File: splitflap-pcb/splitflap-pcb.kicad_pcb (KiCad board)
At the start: 2 copper layers, 50 x 32 mm, 16 parts, among them J1 INPUT CONN, J2 HALL 1, J3 HALL 2, J4 STEPPER 1, J5 STEPPER 2, J6 OUTPUT CONN, J7 AVR-ISP-6, U1 REGULATOR, U2 ATtiny88-AU, U3 TPIC6595

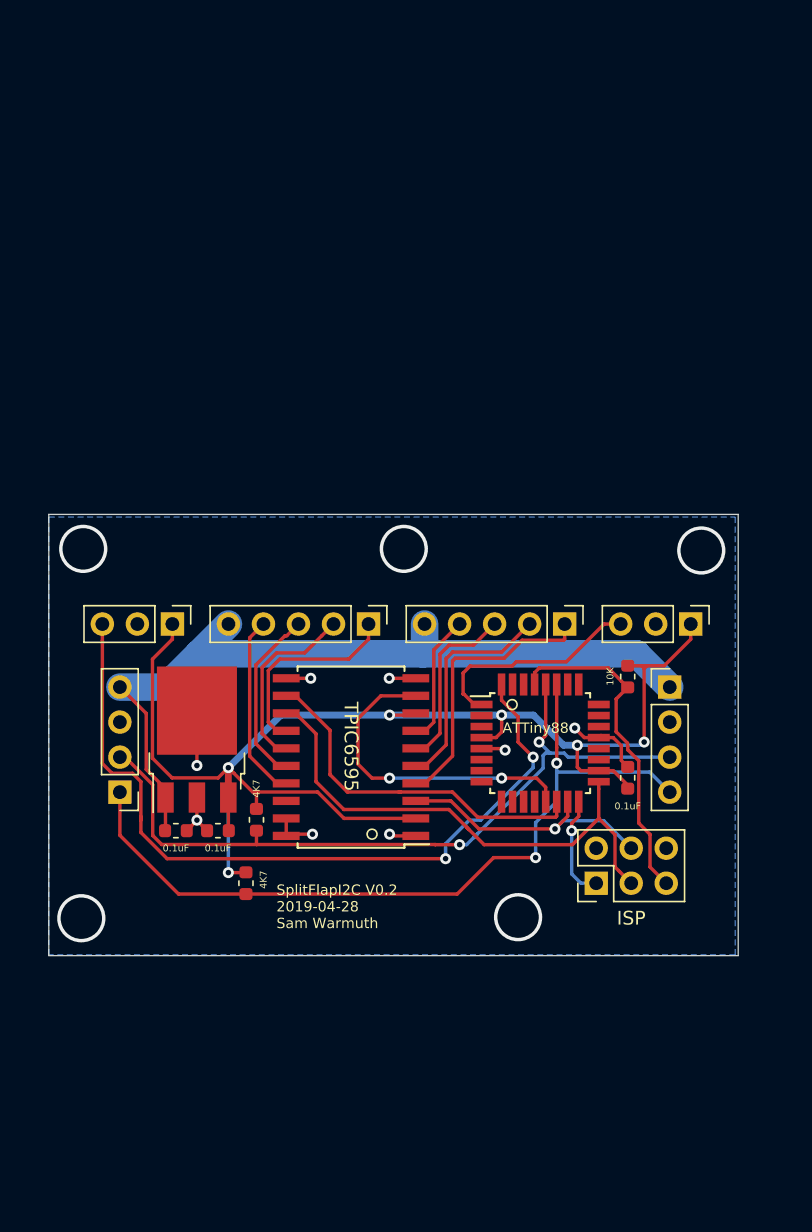
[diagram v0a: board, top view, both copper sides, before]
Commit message: Redesign PCB, connectors are too big
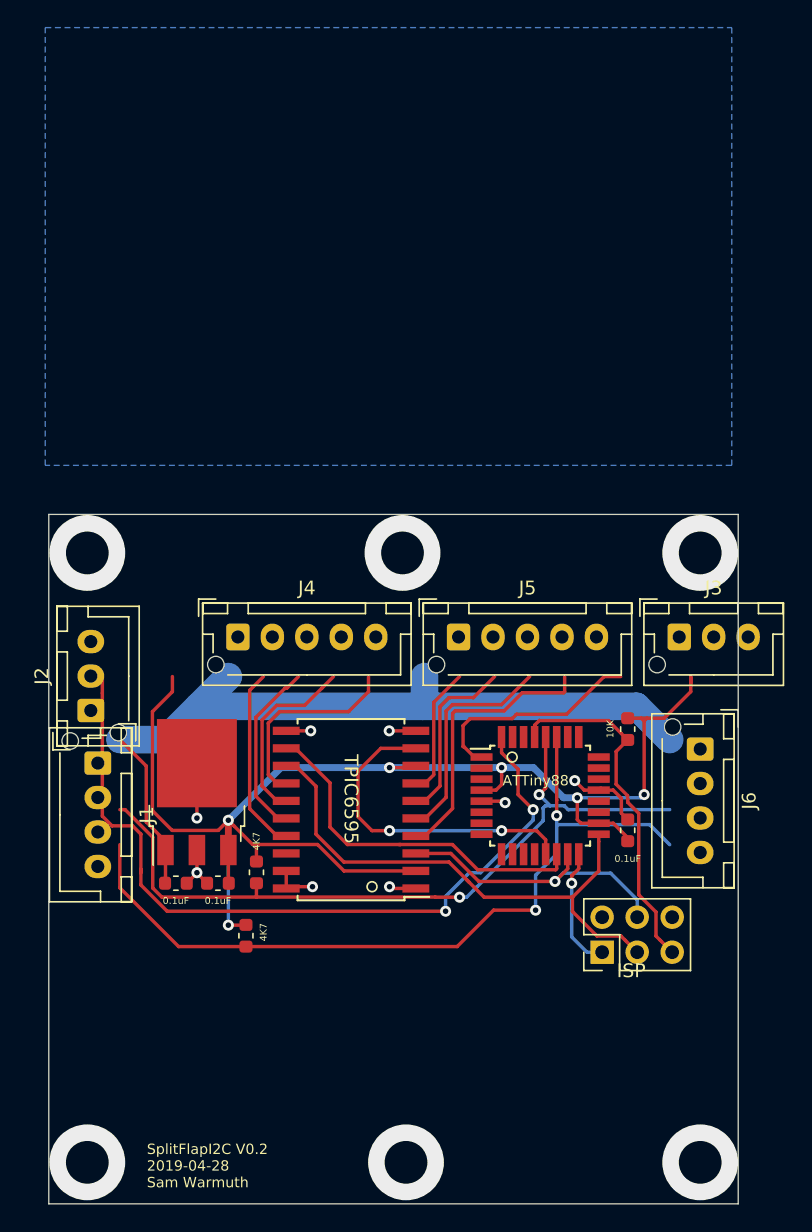
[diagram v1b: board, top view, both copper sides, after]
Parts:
- J1, J6: footprint Connector_PinHeader_2.54mm:PinHeader_1x04_P2.54mm_Vertical -> Connector_JST:JST_XH_B4B-XH-AM_1x04_P2.50mm_Vertical
- J2, J3: footprint Connector_PinHeader_2.54mm:PinHeader_1x03_P2.54mm_Vertical -> Connector_JST:JST_XH_B3B-XH-AM_1x03_P2.50mm_Vertical
- J4, J5: footprint Connector_PinHeader_2.54mm:PinHeader_1x05_P2.54mm_Vertical -> Connector_JST:JST_XH_B5B-XH-AM_1x05_P2.50mm_Vertical
- moved J4 9.52 mm to (113.7, 108.9), turned to 0 degrees
- moved J2 8.62 mm to (103.0, 114.2), turned to 90 degrees
- moved J5 7.75 mm to (129.7, 108.9), turned to 0 degrees
- moved J7 5.02 mm to (140.1, 131.8)
- moved J6 5.01 mm to (147.2, 117.0), turned to 270 degrees
- moved R2 3.81 mm to (114.3, 130.6)
- moved C3 3.81 mm to (142.0, 122.9)
- moved R3 3.81 mm to (115.1, 126.0)
- moved U1 3.81 mm to (110.7, 120.1)
- moved U2 3.81 mm to (135.6, 120.4)
- moved U3 3.81 mm to (121.9, 121.4)
- moved C1 3.81 mm to (112.3, 126.7)
- moved C2 3.81 mm to (109.2, 126.7)
- moved R1 3.81 mm to (142.0, 115.6)
- moved J1 2.65 mm to (103.6, 118.0), turned to 270 degrees
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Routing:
- net +12V: track 58.9 -> 11.8 mm
- net Net-(J2-Pad3): track 57.0 -> 104.1 mm, vias 2 -> 3
- net MOSI: track 19.9 -> 21.6 mm
- net MISO: track 7.50 -> 8.88 mm
- net RST: track 24.4 -> 25.8 mm
- net SCK: track 38.0 -> 39.3 mm
- net GND: vias 13 -> 8
- net (no net): vias 0 -> 5
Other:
- board size 50 x 32 mm -> 50 x 50 mm

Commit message: Getting ready to global delete tracks
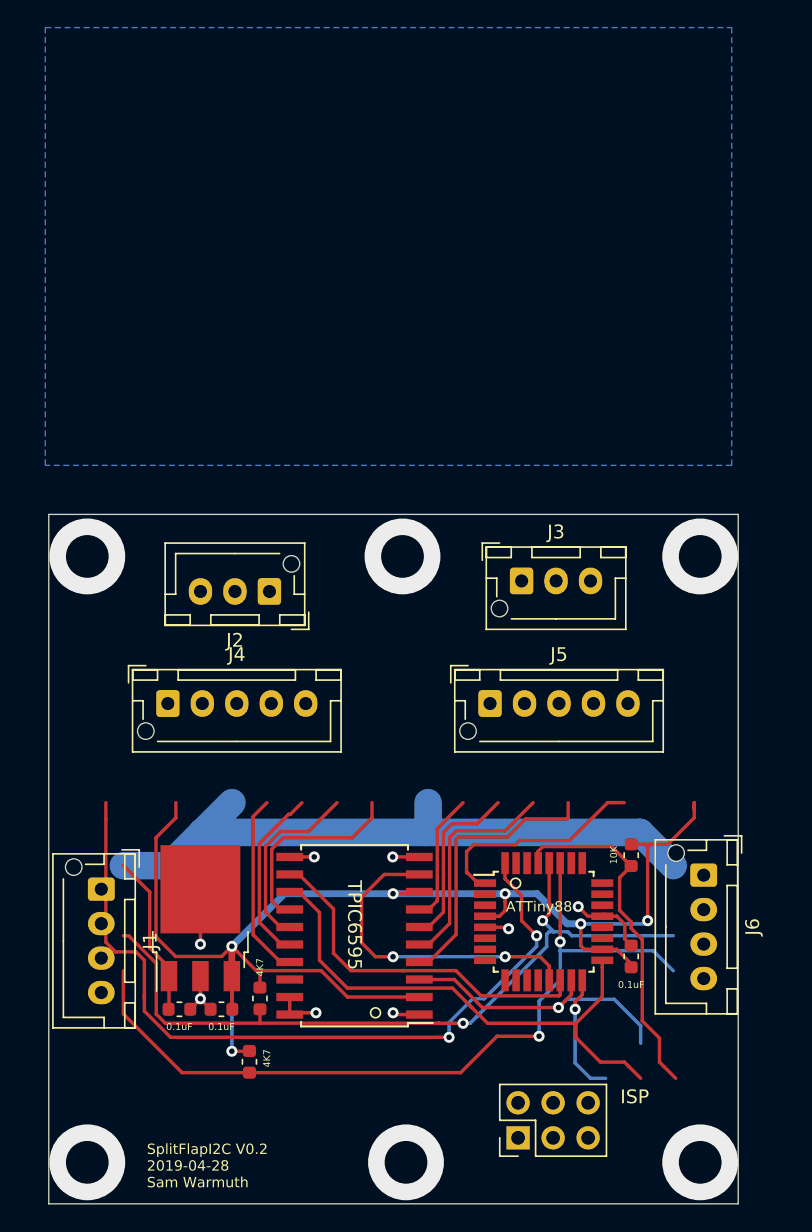
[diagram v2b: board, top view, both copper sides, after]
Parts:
- moved J2 15.6 mm to (116.0, 105.6), turned to 180 degrees
- moved J7 14.8 mm to (134.0, 145.2)
- moved J3 12.1 mm to (134.3, 104.8)
- moved J6 9.15 mm to (147.5, 126.2)
- moved R1 9.15 mm to (142.2, 124.7)
- moved U1 9.15 mm to (111.0, 129.3)
- moved U3 9.15 mm to (122.2, 130.6)
- moved C1 9.15 mm to (112.5, 135.9)
- moved C2 9.15 mm to (109.5, 135.9)
- moved C3 9.15 mm to (142.2, 132.1)
- moved J1 9.15 mm to (103.8, 127.2)
- moved R3 9.15 mm to (115.3, 135.1)
- moved U2 9.15 mm to (135.9, 129.5)
- moved R2 9.15 mm to (114.6, 139.7)
- moved J4 7.01 mm to (108.6, 113.7)
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
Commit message: Actually the correct footprints
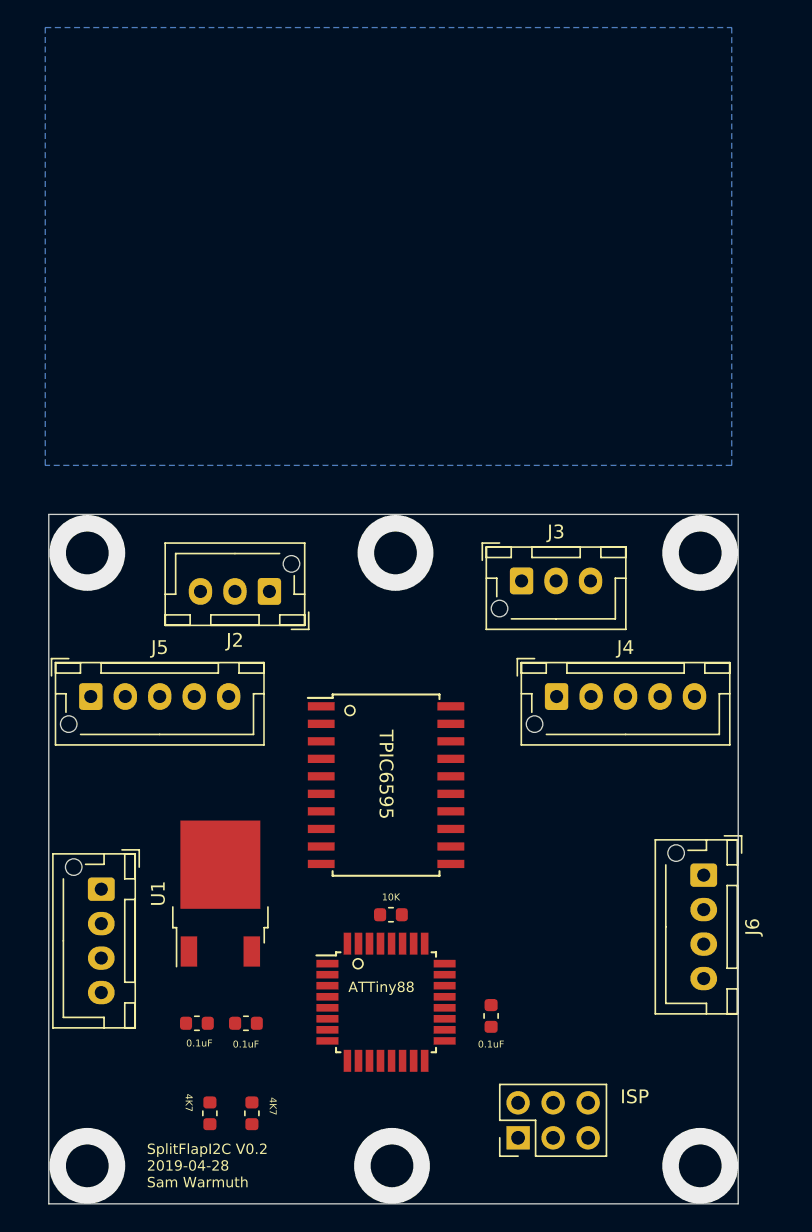
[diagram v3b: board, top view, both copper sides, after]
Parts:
- U1: footprint Package_TO_SOT_SMD:TO-252-3_TabPin2 -> Package_TO_SOT_SMD:TO-252-2
- moved J5 29.0 mm to (103.0, 113.2)
- moved J4 28.2 mm to (136.8, 113.2)
- moved R1 18.0 mm to (124.8, 129.0), turned to 0 degrees
- moved U2 12.8 mm to (124.5, 135.4)
- moved U3 11.2 mm to (124.5, 119.6), turned to 0 degrees
- moved C3 11.0 mm to (132.1, 136.4)
- moved R3 8.35 mm to (114.7, 143.4), turned to 270 degrees
- moved R2 4.71 mm to (111.7, 143.4), turned to 270 degrees
- moved U1 2.30 mm to (112.4, 127.5)
- moved C1 2.05 mm to (114.3, 136.9)
- moved C2 1.63 mm to (110.7, 136.9)
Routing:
- net Net-(J2-Pad3): track 104.1 -> 0.00 mm, vias 3 -> 0
- net +5V: track 103.2 -> 0.00 mm, vias 6 -> 0
- net SDA: track 58.1 -> 0.00 mm, vias 2 -> 0
- net SCL: track 54.9 -> 0.00 mm, vias 2 -> 0
- net SCK: track 39.3 -> 0.00 mm
- net SS: track 26.3 -> 0.00 mm
- net RST: track 25.8 -> 0.00 mm
- net GND: track 25.1 -> 0.00 mm, vias 8 -> 0
- net TPIC-ENABLE: track 24.4 -> 0.00 mm, vias 2 -> 0
- net MOSI: track 21.6 -> 0.00 mm, vias 1 -> 0
- net Net-(J5-Pad1): track 20.3 -> 0.00 mm
- net Net-(J5-Pad2): track 16.2 -> 0.00 mm
- net Net-(J3-Pad3): track 16.1 -> 0.00 mm
- net Net-(J4-Pad1): track 14.6 -> 0.00 mm
- net Net-(J4-Pad3): track 13.6 -> 0.00 mm
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
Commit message: placed components
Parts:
- J1, J6: footprint Connector_JST:JST_XH_B4B-XH-AM_1x04_P2.50mm_Vertical -> Connector_JST:JST_XH_B4B-XH-A_1x04_P2.50mm_Vertical
- J2, J3: footprint Connector_JST:JST_XH_B3B-XH-AM_1x03_P2.50mm_Vertical -> Connector_JST:JST_XH_B3B-XH-A_1x03_P2.50mm_Vertical
- J4, J5: footprint Connector_JST:JST_XH_B5B-XH-AM_1x05_P2.50mm_Vertical -> Connector_JST:JST_XH_B5B-XH-A_1x05_P2.50mm_Vertical
- moved J5 31.2 mm to (134.3, 113.0), turned to 90 degrees
- moved J4 22.4 mm to (114.5, 113.0), turned to 90 degrees
- moved J7 20.9 mm to (135.3, 124.4)
- moved R2 17.4 mm to (117.0, 126.9)
- moved R3 17.1 mm to (119.0, 126.9)
- moved J2 13.4 mm to (103.0, 109.0), turned to 0 degrees
- moved C3 12.4 mm to (132.1, 123.9)
- moved U2 12.3 mm to (126.0, 123.2)
- moved U3 11.8 mm to (125.0, 107.8), turned to 180 degrees
- moved R1 11.8 mm to (124.4, 117.3), turned to 180 degrees
- moved J3 8.69 mm to (141.9, 109.0)
- moved C1 8.48 mm to (113.7, 128.4)
- moved C2 8.46 mm to (110.7, 128.4)
- moved U1 5.41 mm to (112.2, 122.1)
- moved J1 3.27 mm to (103.0, 124.0), turned to 90 degrees
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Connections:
- J6 pad 1: +12V -> SDA
- J6 pad 2: GND -> SCL
- J6 pad 3: SCL -> GND
- J6 pad 4: SDA -> +12V
- U3 pad 14: Net-(J4-Pad1) -> Net-(J4-Pad4)
- U3 pad 15: Net-(J4-Pad2) -> Net-(J4-Pad3)
- U3 pad 16: Net-(J4-Pad3) -> Net-(J4-Pad2)
- U3 pad 17: Net-(J4-Pad4) -> Net-(J4-Pad1)
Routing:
- net GND: vias 0 -> 4
- net (no net): vias 6 -> 0
- removed copper zone on B.Cu, net GND
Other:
- board size 50 x 50 mm -> 50 x 33.3 mm
- board text added: "SplitFlapI2C V0.3 2019-04-29 Sam Warmuth"
- board text removed: "SplitFlapI2C V0.2 2019-04-28 Sam Warmuth"

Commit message: Wired
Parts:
- added C4: 0.1uF, Capacitor_SMD:C_0603_1608Metric, F.Cu at (129.5, 115.7)
- moved R1 12.7 mm to (127.9, 129.5), turned to 0 degrees
- moved C3 12.4 mm to (119.8, 122.6), turned to 270 degrees
- moved J7 3.82 mm to (139.1, 124.1), turned to 180 degrees
- moved U1 1.27 mm to (112.2, 123.4)
- moved C1 1.27 mm to (113.7, 129.7)
- moved C2 1.27 mm to (110.7, 129.7)
- moved R2 0.25 mm to (117.3, 126.9), turned to 90 degrees
- moved R3 0.25 mm to (119.3, 126.9)
- moved J5 0.21 mm to (134.5, 113.0)
- moved U2 0.18 mm to (125.8, 123.3), turned to 180 degrees
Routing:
- net +5V: track 0.00 -> 108.7 mm, vias 0 -> 6
- net +12V: track 0.00 -> 81.4 mm
- net SDA: track 0.00 -> 53.8 mm
- net Net-(J2-Pad3): track 0.00 -> 53.5 mm, vias 0 -> 2
- net SCL: track 0.00 -> 51.8 mm, vias 0 -> 5
- net SCK: track 0.00 -> 38.2 mm, vias 0 -> 2
- net Net-(J3-Pad3): track 0.00 -> 36.0 mm, vias 0 -> 2
- net MOSI: track 0.00 -> 28.7 mm, vias 0 -> 4
- net GND: track 0.00 -> 28.3 mm, vias 4 -> 15
- net RST: track 0.00 -> 26.4 mm
- net MISO: track 0.00 -> 18.8 mm, vias 0 -> 2
- net TPIC-ENABLE: track 0.00 -> 18.1 mm
- net SS: track 0.00 -> 17.9 mm
- net Net-(J4-Pad1): track 0.00 -> 7.17 mm
- net Net-(J4-Pad2): track 0.00 -> 6.66 mm
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- added copper zone on B.Cu, net GND

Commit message: Closer, working on stitching
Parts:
- added H1: MountingHole_Pad, MountingHole:MountingHole_3.2mm_M3_Pad, F.Cu at (146.0, 104.1)
- added H2: MountingHole_Pad, MountingHole:MountingHole_3.2mm_M3_Pad, F.Cu at (104.1, 129.2)
- added H3: MountingHole_Pad, MountingHole:MountingHole_3.2mm_M3_Pad, F.Cu at (104.1, 104.1)
- added H4: MountingHole_Pad, MountingHole:MountingHole_3.2mm_M3_Pad, F.Cu at (146.0, 129.2)
- J1, J6: footprint Connector_JST:JST_XH_B4B-XH-A_1x04_P2.50mm_Vertical -> splitflap-pcb:TE_640456-4
- J2, J3: footprint Connector_JST:JST_XH_B3B-XH-A_1x03_P2.50mm_Vertical -> splitflap-pcb:TE_640456-3
- moved J3 4.26 mm to (145.2, 111.7)
- moved J2 3.09 mm to (104.6, 111.7)
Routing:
- net GND: track 28.3 -> 17.7 mm, vias 15 -> 80
- net Net-(J2-Pad3): track 53.5 -> 47.7 mm
- net +5V: track 108.7 -> 110.4 mm, vias 6 -> 5
- net +12V: track 81.4 -> 79.8 mm
- net Net-(J3-Pad3): track 36.0 -> 37.5 mm
- added copper zone on F.Cu, net GND
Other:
- board text added: "12V/I2C"
- board text added: "Hall Sensor 1"
- board text added: "Hall Sensor 2"
- board text added: "NCV78M05"
- board text added: "SplitFlapI2C V0.4 2019-04-29 Sam Warmuth"
- board text added: "Stepper 1"
- board text added: "Stepper 2"
- board text removed: "SplitFlapI2C V0.3 2019-04-29 Sam Warmuth"

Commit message: new netlist
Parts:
- added C5: 0.1uF, Capacitor_SMD:C_0603_1608Metric, F.Cu at (132.3, 123.7)
- added C6: 0.1uF, Capacitor_SMD:C_0603_1608Metric, F.Cu at (131.9, 103.8)
- moved C4 0.20 mm to (129.5, 115.5)
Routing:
- net +5V: track 110.4 -> 116.7 mm, vias 5 -> 7
- net GND: track 17.7 -> 23.7 mm, vias 80 -> 198
- net Net-(J7-Pad2): vias 0 -> 1
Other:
- board text added: "SplitFlapI2C V0.5 2019-04-30 Sam Warmuth"
- board text removed: "SplitFlapI2C V0.4 2019-04-29 Sam Warmuth"

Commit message: More
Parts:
- moved C4 3.31 mm to (131.7, 113.1), turned to 270 degrees
- moved J5 0.86 mm to (135.4, 113.0)
- moved J4 0.79 mm to (113.7, 113.0)
- moved C6 0.18 mm to (131.7, 103.8), turned to 90 degrees
- turned R3 to 90 degrees
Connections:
- net Net-(J2-Pad3) renamed HALL1SIG
- net Net-(J3-Pad3) renamed HALL2SIG
- C4 pad 1: GND -> +5V
- C4 pad 2: +5V -> GND
- C6 pad 1: GND -> +5V
- C6 pad 2: +5V -> GND
- R3 pad 1: SCL -> +5V
- R3 pad 2: +5V -> SCL
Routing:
- net +5V: track 116.7 -> 112.5 mm
- net +12V: track 80.1 -> 83.0 mm
- net GND: track 23.7 -> 21.5 mm, vias 198 -> 194
- net Net-(J5-Pad4): track 4.98 -> 6.97 mm
- net Net-(J4-Pad2): track 6.66 -> 7.57 mm
- net Net-(J5-Pad3): track 5.13 -> 5.98 mm
- net Net-(J5-Pad2): track 5.64 -> 6.49 mm
- net Net-(J5-Pad1): track 6.15 -> 7.00 mm
- net Net-(J4-Pad1): track 7.17 -> 7.96 mm
- net Net-(J4-Pad4): track 6.00 -> 6.79 mm
- net Net-(J4-Pad3): track 6.15 -> 6.94 mm
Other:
- board text added: "SplitFlapI2C V0.6 2019-04-30 Sam Warmuth"
- board text removed: "SplitFlapI2C V0.5 2019-04-30 Sam Warmuth"
